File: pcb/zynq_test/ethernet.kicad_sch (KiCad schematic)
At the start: 1 part

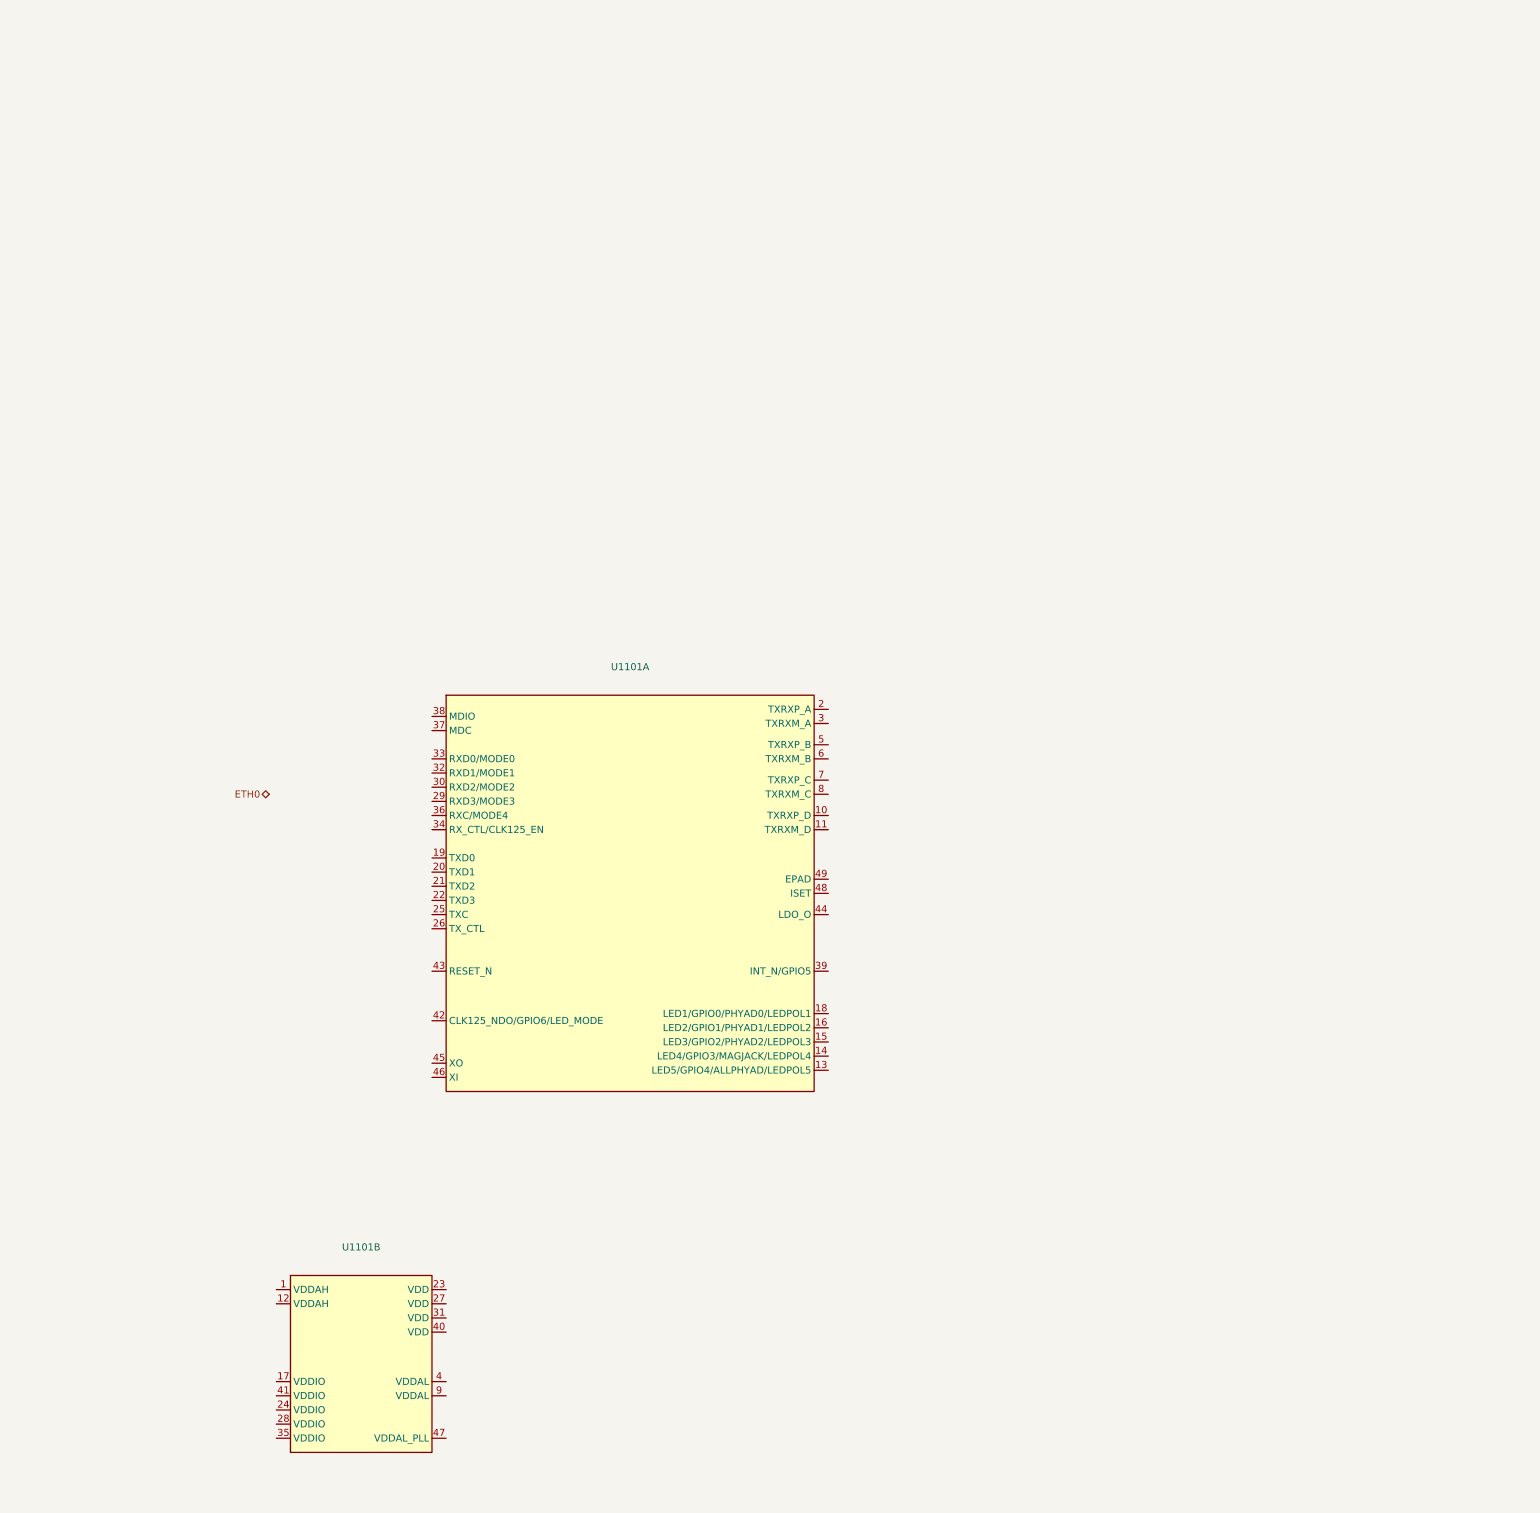
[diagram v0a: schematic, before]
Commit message: Finished Ethernet, swapped FTDI chip for QFN
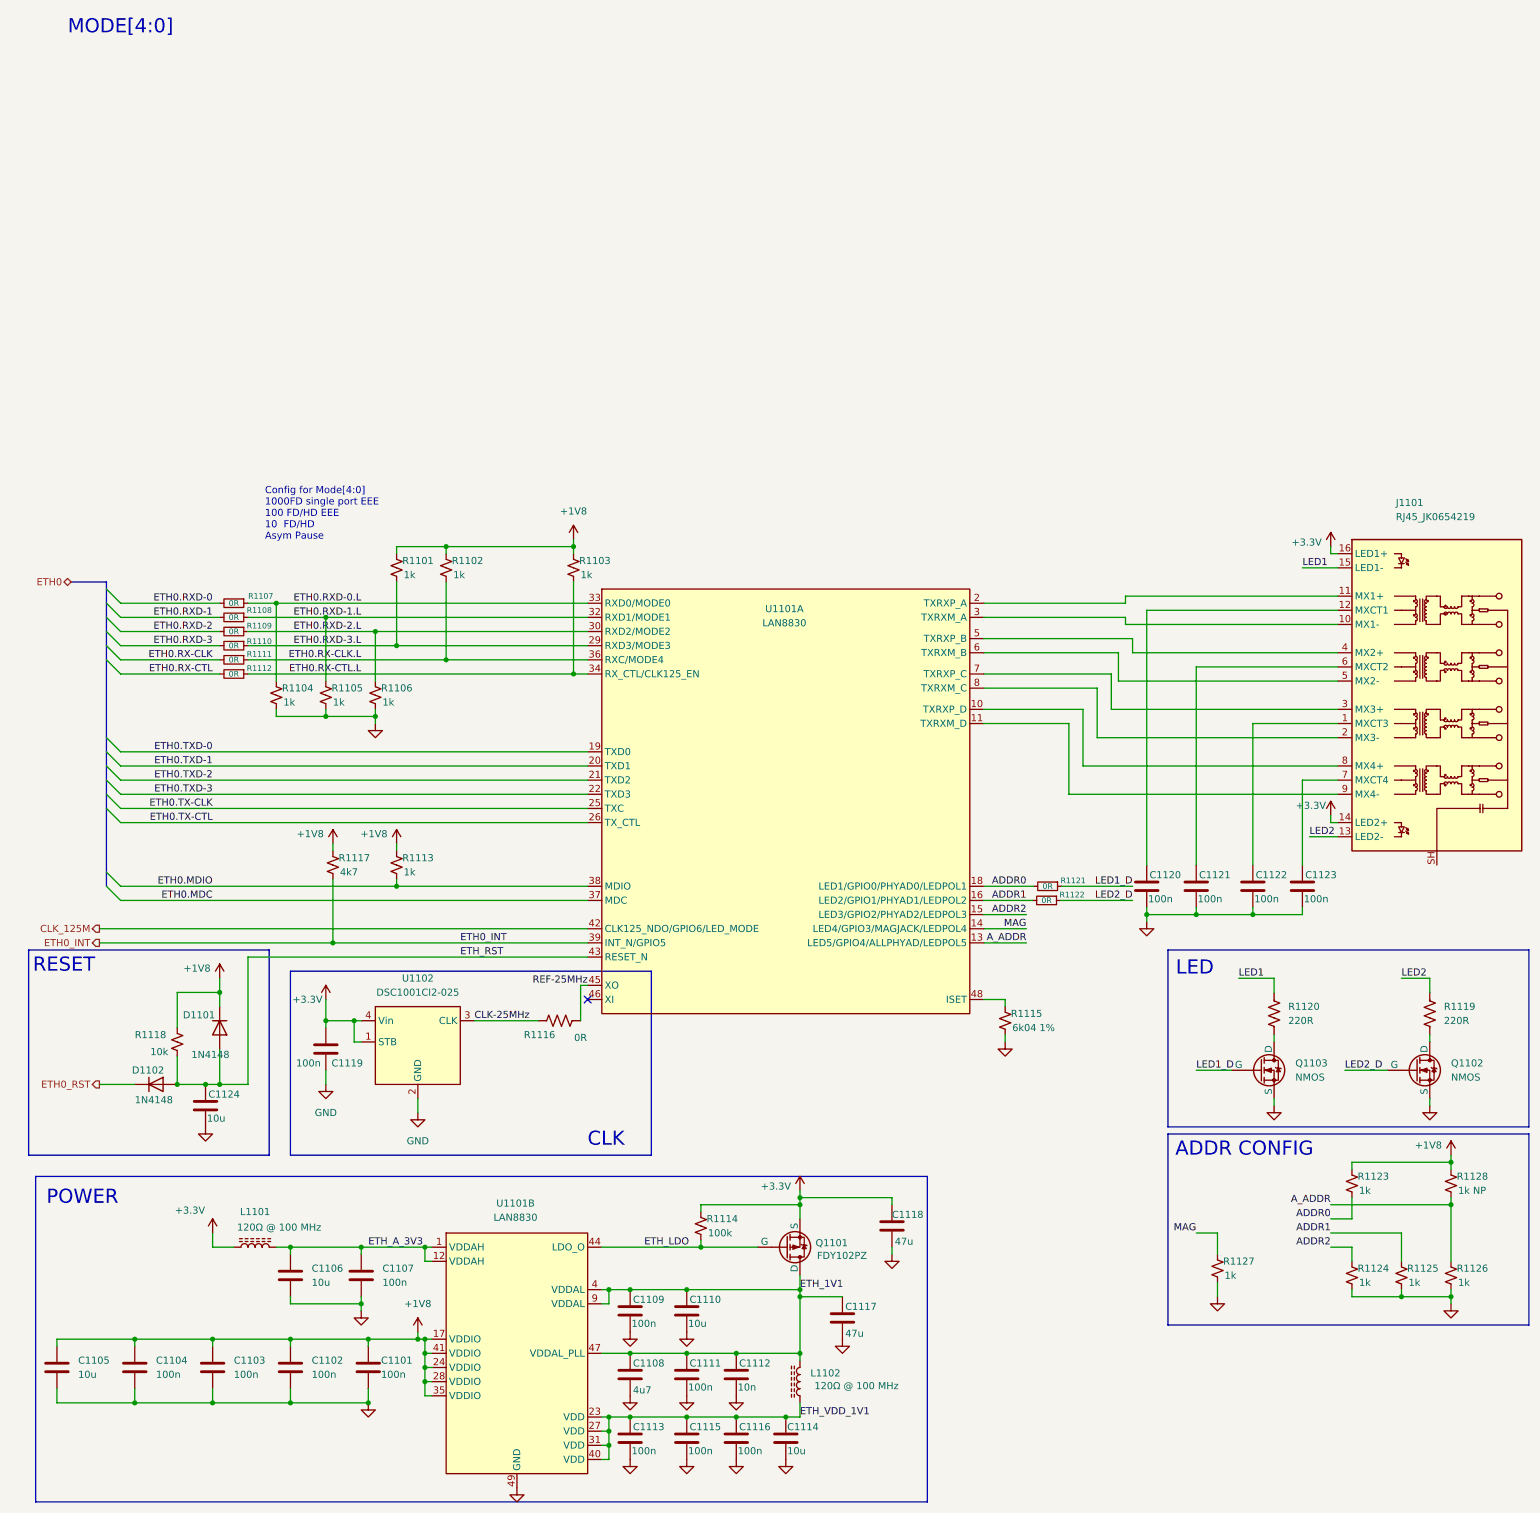
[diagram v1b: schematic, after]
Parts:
- added C1101, C1102, C1103, C1104, C1107, C1109, C1111, C1113, C1115, C1116, C1119, C1120, C1121, C1122, C1123: 100n, symbol Device:C
- added C1105, C1106, C1110, C1114, C1124: 10u, symbol Device:C
- added C1108: 4u7, symbol Device:C
- added C1112: 10n, symbol Device:C
- added C1117, C1118: 47u, symbol Device:C
- added D1101, D1102: 1N4148, symbol Device:D
- added J1101: RJ45_JK0654219, Connector_RJ:RJ45_Pulse_JK0654219NL_Horizontal, symbol Connector:RJ45_JK0654219
- added L1101, L1102: 120Ω @ 100 MHz, symbol Device:L_Ferrite
- added Q1101: FDY102PZ, symbol Simulation_SPICE:PMOS
- added Q1102, Q1103: NMOS, symbol Simulation_SPICE:NMOS
- added R1101, R1102, R1103, R1104, R1105, R1106, R1113, R1123, R1124, R1125, R1126, R1127: 1k, symbol Device:R_Small_US
- added R1107, R1108, R1109, R1110, R1111, R1112, R1121, R1122: 0R, symbol Device:R_Small
- added R1114: 100k, symbol Device:R_Small_US
- added R1115: 6k04 1%, symbol Device:R_Small_US
- added R1116: 0R, symbol Device:R_US
- added R1117: 4k7, symbol Device:R_Small_US
- added R1118: 10k, symbol Device:R_Small_US
- added R1119, R1120: 220R, symbol Device:R_US
- added R1128: 1k NP, symbol Device:R_Small_US
- added U1102: DSC1001CI2-025, symbol other:DSC1001CI2-033.3300
- U1101: value ~ -> LAN8830
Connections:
- net at U1101.10 (TXRXP_D): now also J1101.8 (MX4+)
- net at U1101.11 (TXRXM_D): now also J1101.9 (MX4-)
- net A_ADDR: now reaches U1101.13 (LED5/GPIO4/ALLPHYAD/LEDPOL5)
- net A_ADDR: now also R1126.1, R1128.2
- net MAG: now reaches U1101.14 (LED4/GPIO3/MAGJACK/LEDPOL4)
- net MAG: now also R1127.1
- net ADDR2: now reaches U1101.15 (LED3/GPIO2/PHYAD2/LEDPOL3)
- net ADDR2: now also R1124.1
- net ADDR1: now reaches U1101.16 (LED2/GPIO1/PHYAD1/LEDPOL2)
- net ADDR1: now also R1122.2, R1125.1
- net ADDR0: now reaches U1101.18 (LED1/GPIO0/PHYAD0/LEDPOL1)
- net ADDR0: now also R1121.2, R1123.2
- net ETH0.TXD-0: now reaches U1101.19 (TXD0)
- net at U1101.2 (TXRXP_A): now also J1101.11 (MX1+)
- net ETH0.TXD-1: now reaches U1101.20 (TXD1)
- net ETH0.TXD-2: now reaches U1101.21 (TXD2)
- net ETH0.TXD-3: now reaches U1101.22 (TXD3)
- net ETH0.TX-CLK: now reaches U1101.25 (TXC)
- net ETH0.TX-CTL: now reaches U1101.26 (TX_CTL)
- net ETH0.RXD-3.L: now reaches U1101.29 (RXD3/MODE3)
- net ETH0.RXD-3.L: now also R1101.2, R1110.1
- net at U1101.3 (TXRXM_A): now also J1101.10 (MX1-)
- net ETH0.RXD-2.L: now reaches U1101.30 (RXD2/MODE2)
- net ETH0.RXD-2.L: now also R1106.1, R1109.1
- net ETH0.RXD-1.L: now reaches U1101.32 (RXD1/MODE1)
- net ETH0.RXD-1.L: now also R1105.1, R1108.1
- net ETH0.RXD-0.L: now reaches U1101.33 (RXD0/MODE0)
- net ETH0.RXD-0.L: now also R1104.1, R1107.1
- net ETH0.RX-CTL.L: now reaches U1101.34 (RX_CTL/CLK125_EN)
- net ETH0.RX-CTL.L: now also R1103.2, R1112.1
- net ETH0.RX-CLK.L: now reaches U1101.36 (RXC/MODE4)
- net ETH0.RX-CLK.L: now also R1102.2, R1111.1
- net ETH0.MDC: now reaches U1101.37 (MDC)
- net ETH0.MDIO: now reaches U1101.38 (MDIO)
- net ETH0.MDIO: now also R1113.2
- net ETH0_INT: now reaches U1101.39 (INT_N/GPIO5)
- net ETH0_INT: now also R1117.2
- net CLK_125M: now reaches U1101.42 (CLK125_NDO/GPIO6/LED_MODE)
- net ETH_RST: now reaches U1101.43 (RESET_N)
- net ETH_RST: now also C1124.1, D1101.2 (A), D1102.2 (A), R1118.2
- net REF-25MHz: now reaches U1101.45 (XO)
- net REF-25MHz: now also R1116.2
- net at U1101.48 (ISET): now also R1115.1
- net at U1101.5 (TXRXP_B): now also J1101.4 (MX2+)
- net at U1101.6 (TXRXM_B): now also J1101.5 (MX2-)
- net at U1101.7 (TXRXP_C): now also J1101.3 (MX3+)
- net at U1101.8 (TXRXM_C): now also J1101.2 (MX3-)
- net ETH_A_3V3: now reaches U1101.1 (VDDAH)
- net ETH_A_3V3: now also U1101.12 (VDDAH), C1106.1, C1107.1, L1101.2
- net +1V8: now reaches U1101.17 (VDDIO)
- net +1V8: now also U1101.24 (VDDIO), U1101.28 (VDDIO), U1101.35 (VDDIO), U1101.41 (VDDIO), C1101.1, C1102.1, C1103.1, C1104.1, C1105.1, D1101.1 (K), R1101.1, R1102.1, R1103.1, R1113.1, R1117.1, R1118.1, R1123.1, R1128.1
- net ETH_VDD_1V1: now reaches U1101.23 (VDD)
- net ETH_VDD_1V1: now also U1101.27 (VDD), U1101.31 (VDD), U1101.40 (VDD), C1113.1, C1114.1, C1115.1, C1116.1, L1102.1
- net ETH_1V1: now reaches U1101.4 (VDDAL)
- net ETH_1V1: now also U1101.47 (VDDAL_PLL), U1101.9 (VDDAL), C1108.1, C1109.1, C1110.1, C1111.1, C1112.1, C1117.1, L1102.2, Q1101.3 (D)
- new net: C1122.1, J1101.1 (MXCT3)
- new net: C1123.1, J1101.7 (MXCT4)
- new net: C1120.1, J1101.12 (MXCT1)
- new net: Q1102.1 (D), R1119.2
- new net: Q1103.1 (D), R1120.2
- new net: C1121.1, J1101.6 (MXCT2)
- new net +3.3V: C1118.1, C1119.1, J1101.14 (LED2+), J1101.16 (LED1+), L1101.1, Q1101.2 (S), R1114.1, U1102.1 (STB), U1102.4 (Vin)
- new net CLK-25MHz: R1116.1, U1102.3 (CLK)
- new net ETH0.RX-CLK: R1111.2
- new net ETH0.RX-CTL: R1112.2
- new net ETH0.RXD-0: R1107.2
- new net ETH0.RXD-1: R1108.2
- new net ETH0.RXD-2: R1109.2
- new net ETH0.RXD-3: R1110.2
- new net ETH0_RST: D1102.1 (K)
- new net ETH_LDO: Q1101.1 (G), R1114.2, U1101.44 (LDO_O)
- new net GND: C1101.2, C1102.2, C1103.2, C1104.2, C1105.2, C1106.2, C1107.2, C1108.2, C1109.2, C1110.2, C1111.2, C1112.2, C1113.2, C1114.2, C1115.2, C1116.2, C1117.2, C1118.2, C1119.2, C1120.2, C1121.2, C1122.2, C1123.2, C1124.2, Q1102.3 (S), Q1103.3 (S), R1104.2, R1105.2, R1106.2, R1115.2, R1124.2, R1125.2, R1126.2, R1127.2, U1101.49 (GND), U1102.2 (GND)
- new net LED1: J1101.15 (LED1-), R1120.1
- new net LED1_D: Q1103.2 (G), R1121.1
- new net LED2: J1101.13 (LED2-), R1119.1
- new net LED2_D: Q1102.2 (G), R1122.1
- no-connect marks 0 -> 1
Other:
- note added: "ADDR CONFIG"
- note added: "CLK"
- note added: "Config for Mode[4:0] 1000FD single port EEE 100 FD/HD EEE 10 FD/HD Asym Pause"
- note added: "LED"
- note added: "MODE[4:0]"
- note added: "POWER"
- note added: "RESET"
